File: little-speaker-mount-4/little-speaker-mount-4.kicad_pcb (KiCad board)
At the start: 2 copper layers, 225 x 150 mm, 16 parts

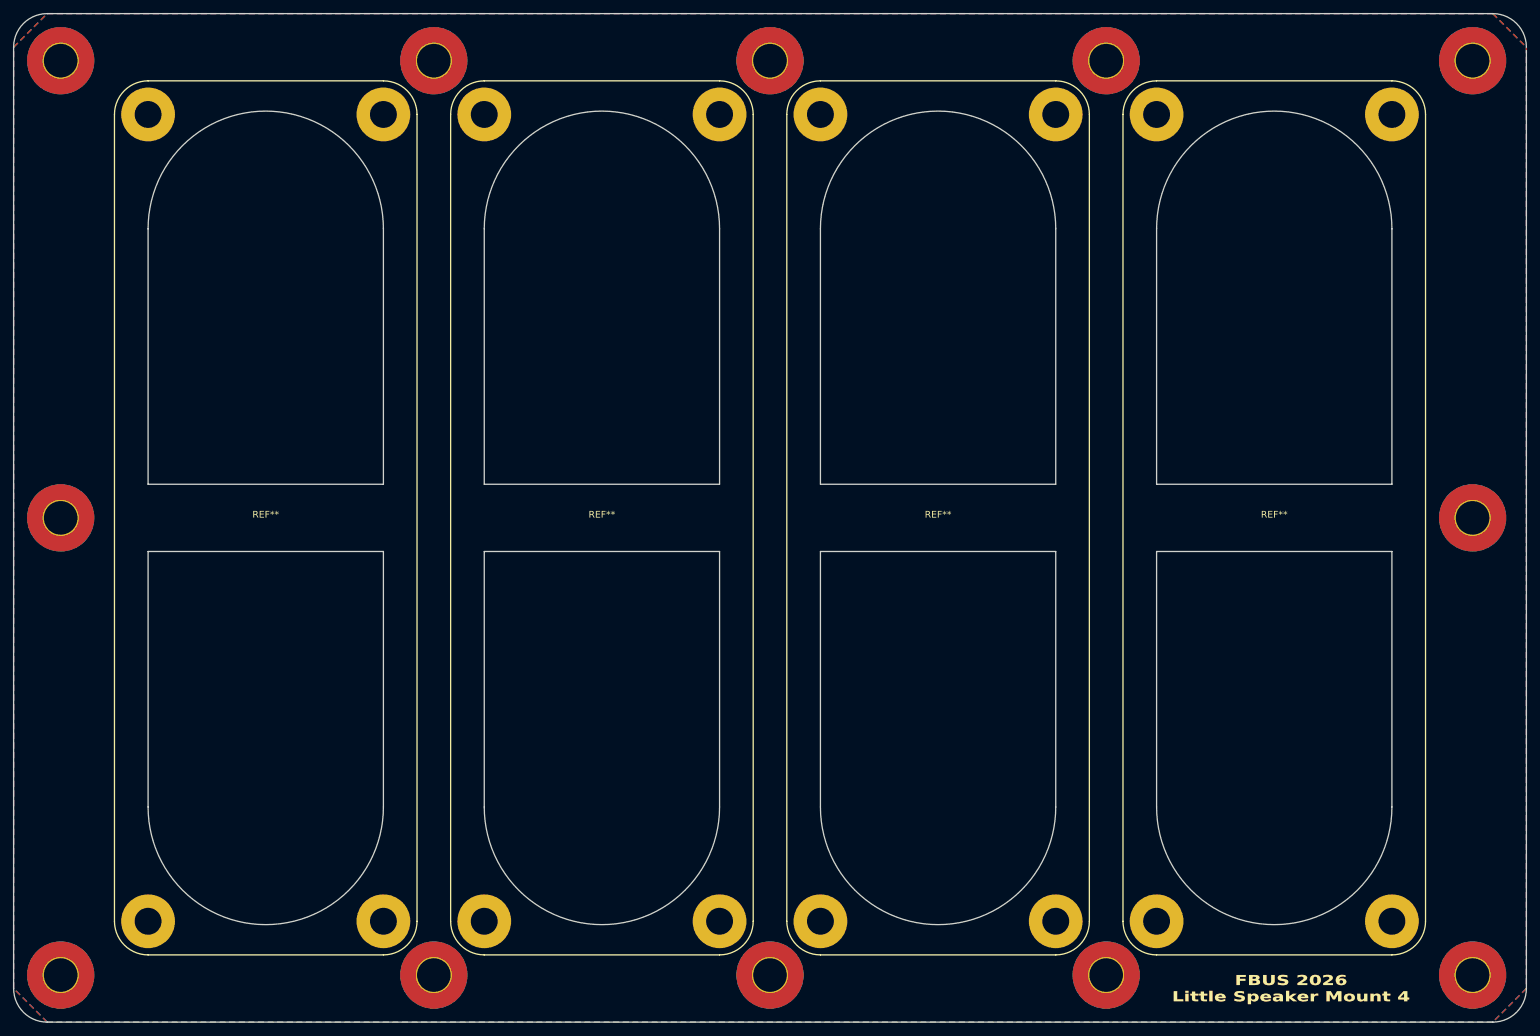
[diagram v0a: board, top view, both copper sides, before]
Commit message: Updated the speaker mount to be better for wood cutting.
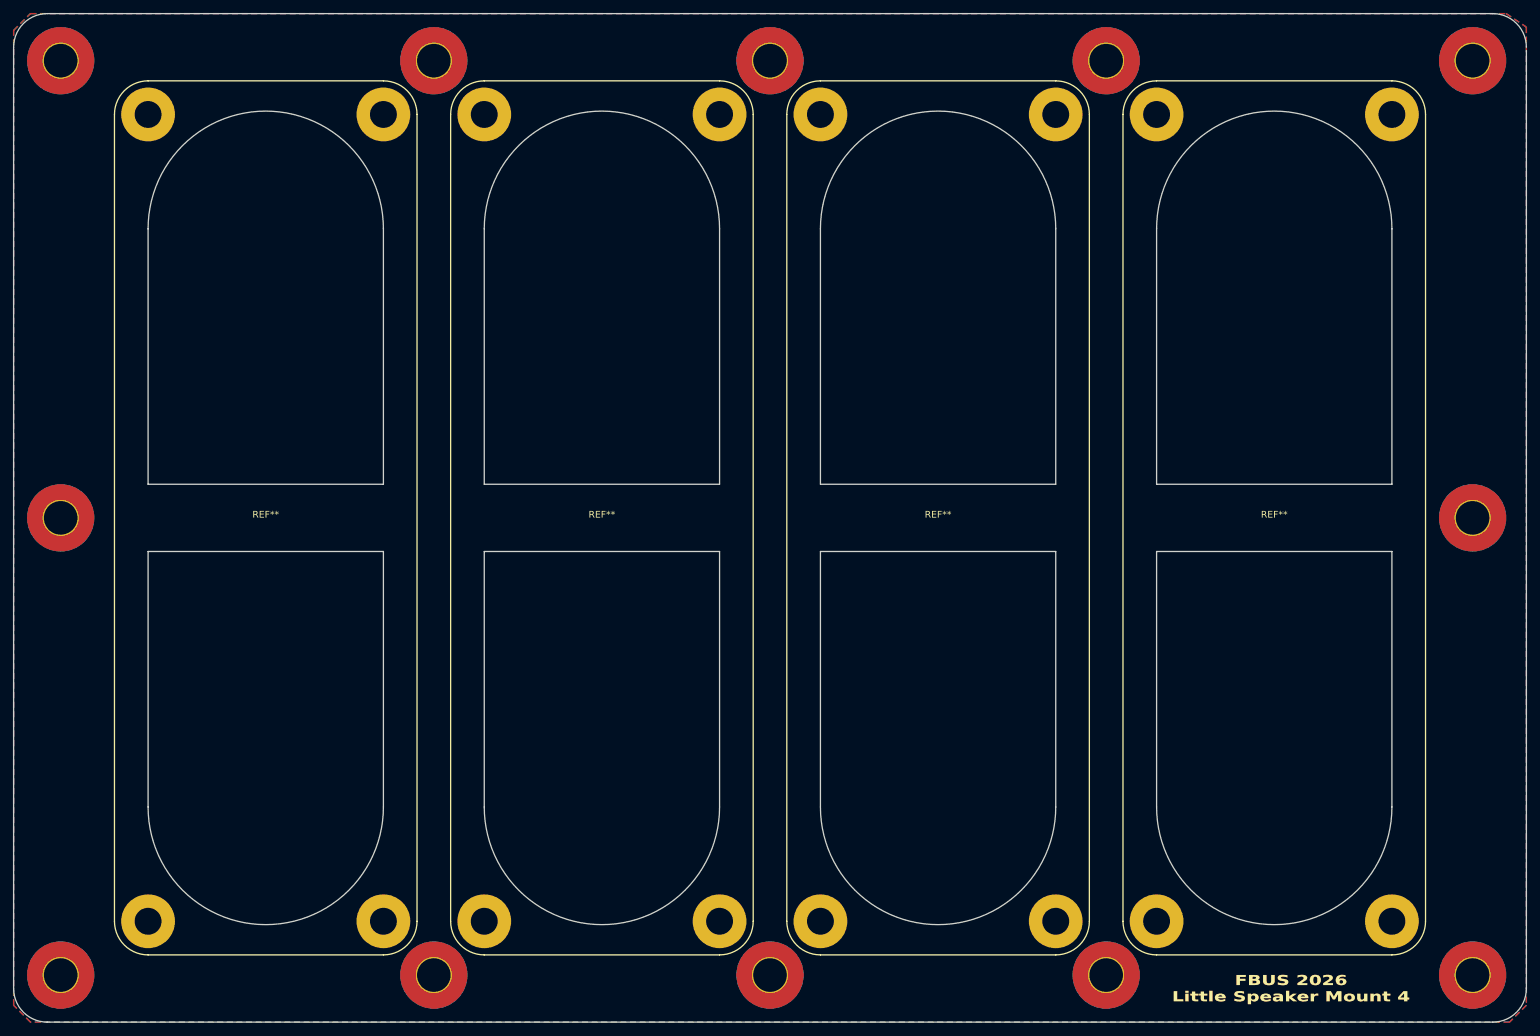
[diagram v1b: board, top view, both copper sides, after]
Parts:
- REF** (x4): footprint speakers:5 1_8 x 1 3_4 inch mini speaker mount -> speakers:5 1_8 x 1 3_4 inch mini speaker mount no keepout
